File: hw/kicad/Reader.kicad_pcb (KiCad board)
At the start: 2 copper layers, 45.3 x 50.2 mm, 61 parts, among them CN1 CN_1X3M, CN2 CN_USB-C, CN3 CN_1X2M, M1 MOD_RFID_NFC_PN532, Q1 TRS_NPN_123, Q2 TRS_NPN_123, Q3 TRS_NPN_123, Q4 TRS_NPN_123, SW1 Tact_Switch, SW2 Tact_Switch_2pin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

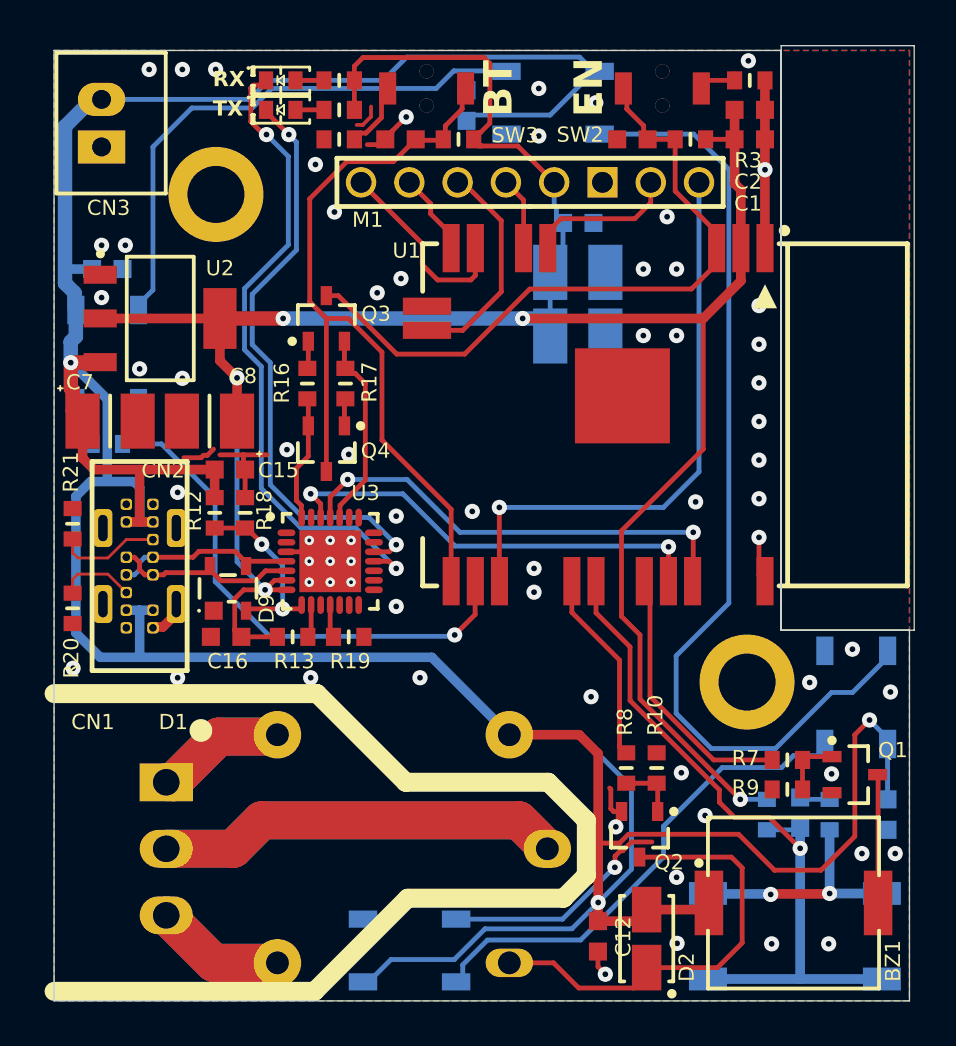
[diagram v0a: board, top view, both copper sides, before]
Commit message: Fixes to make board suitable for local manucatruing
- Track made 0.2 min
- Pads 0.2 min(CP2102)
- Another bug fixes...
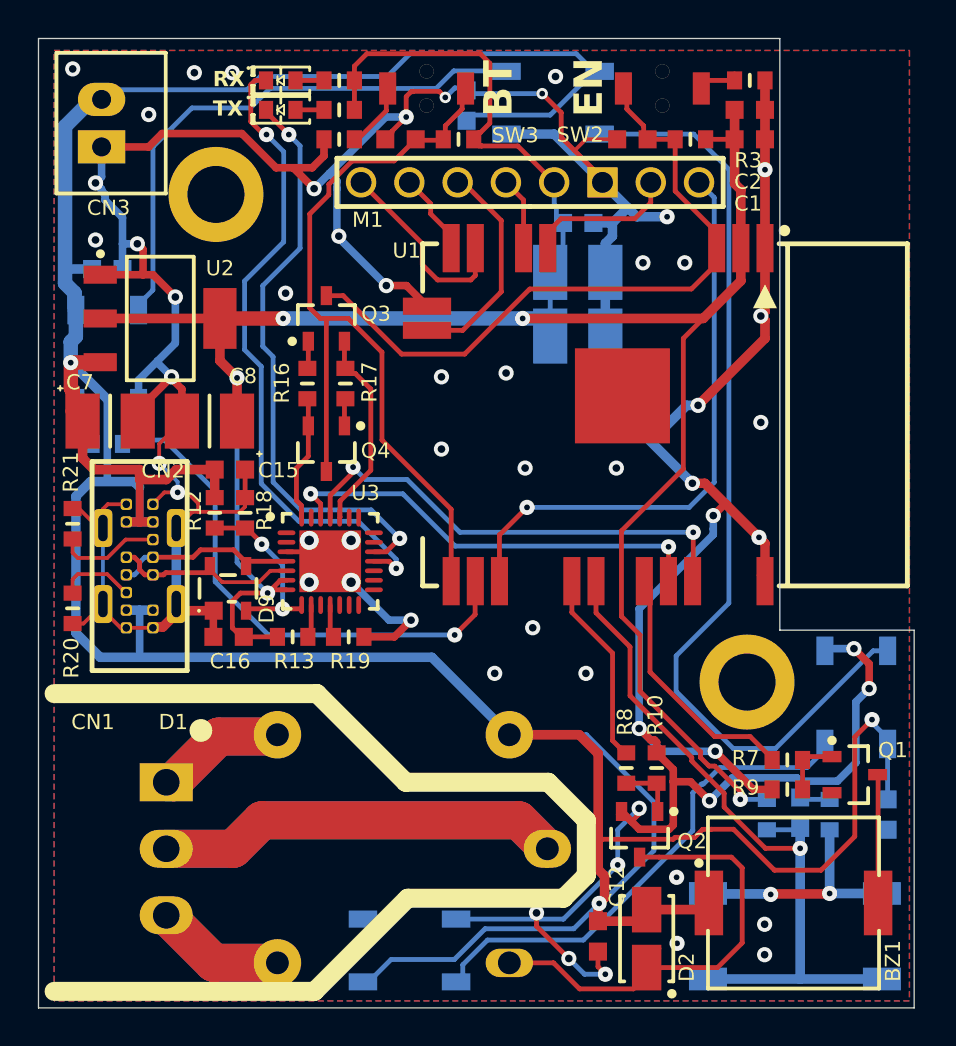
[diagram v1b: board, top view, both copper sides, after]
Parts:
- moved C16 0.13 mm to (135.1, 111.0)
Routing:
- net GND: track 44.7 -> 257.3 mm, vias 68 -> 56
- net 5V: track 196.5 -> 199.3 mm
- net NetD5_2: track 51.6 -> 50.7 mm
- net UART_Tx: track 24.3 -> 25.1 mm
- net buzzer: track 14.0 -> 13.3 mm
- net 3V3: track 132.5 -> 133.1 mm
- net SPI_RST: track 30.4 -> 31.0 mm
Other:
- board size 45.3 x 50.2 mm -> 46.1 x 51 mm
